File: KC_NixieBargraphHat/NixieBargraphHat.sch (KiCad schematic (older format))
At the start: 16 parts, among them J1 Screw_Terminal_1x03, J2 Screw_Terminal_1x02, Q1 FDD18N20LZ, Q2 2N7002, U1 MCP6411, U2 Raspberry_PI_Zero_Header

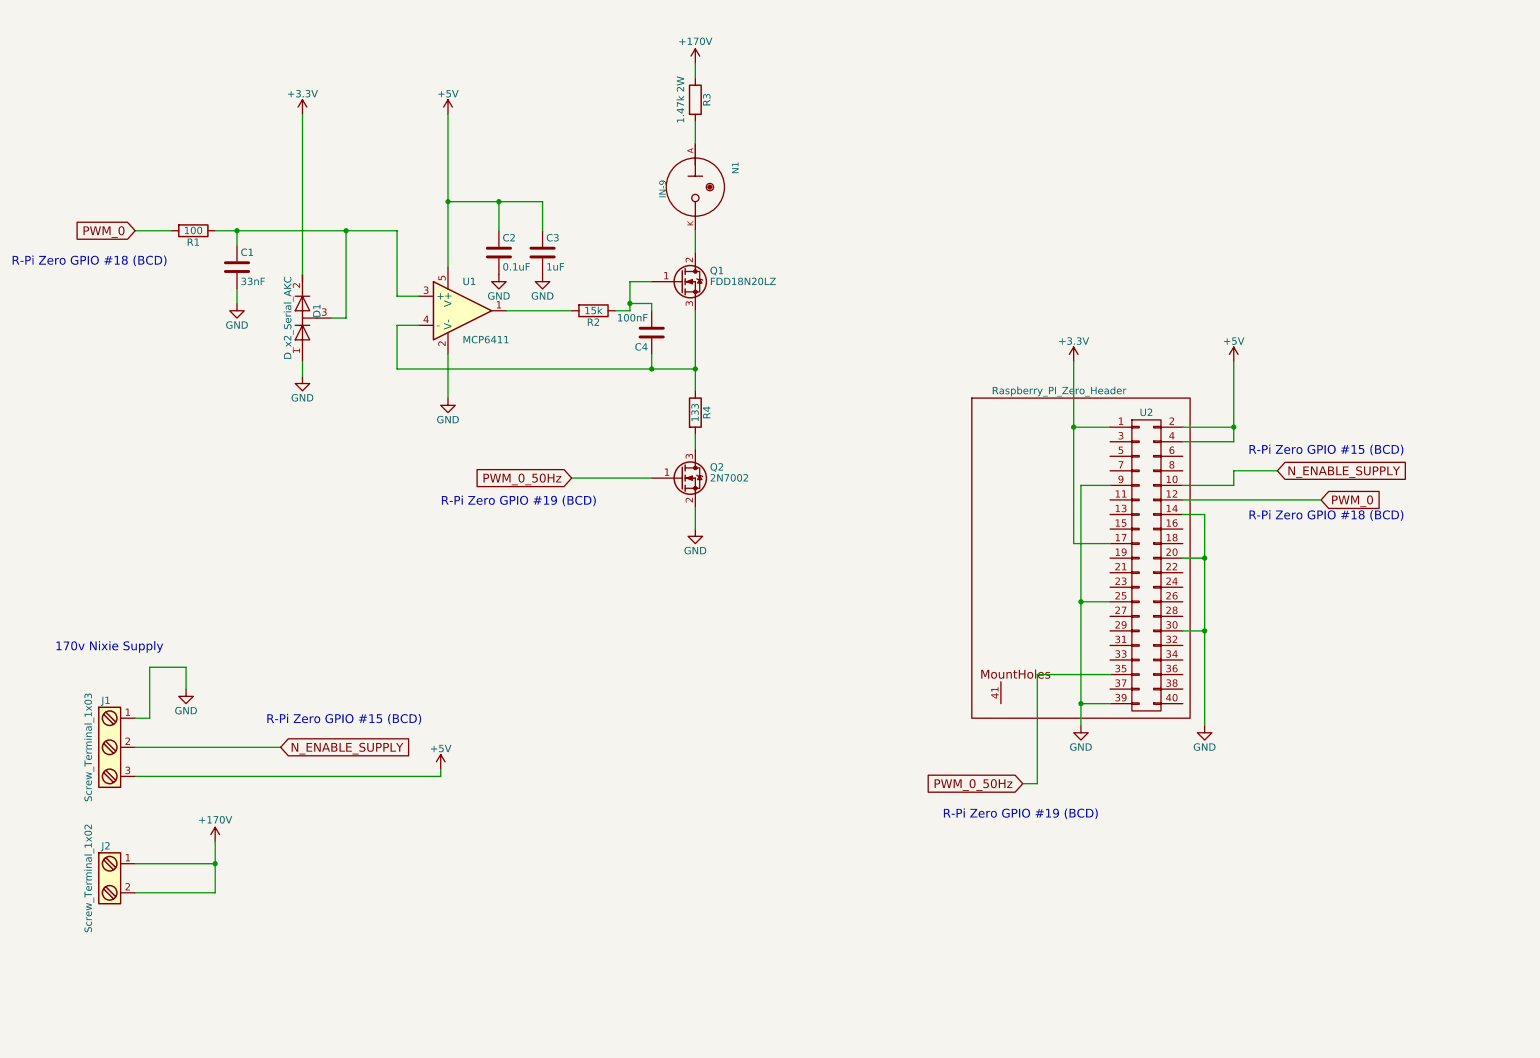
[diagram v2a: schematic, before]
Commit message: Adjusted the schematic to have two channels for the Left and Right Nixie. Also adjusted the PWM to have hardware PWM for the cathod signals, but the low frequency dimming will be done with the 50 Hz low frequency signals
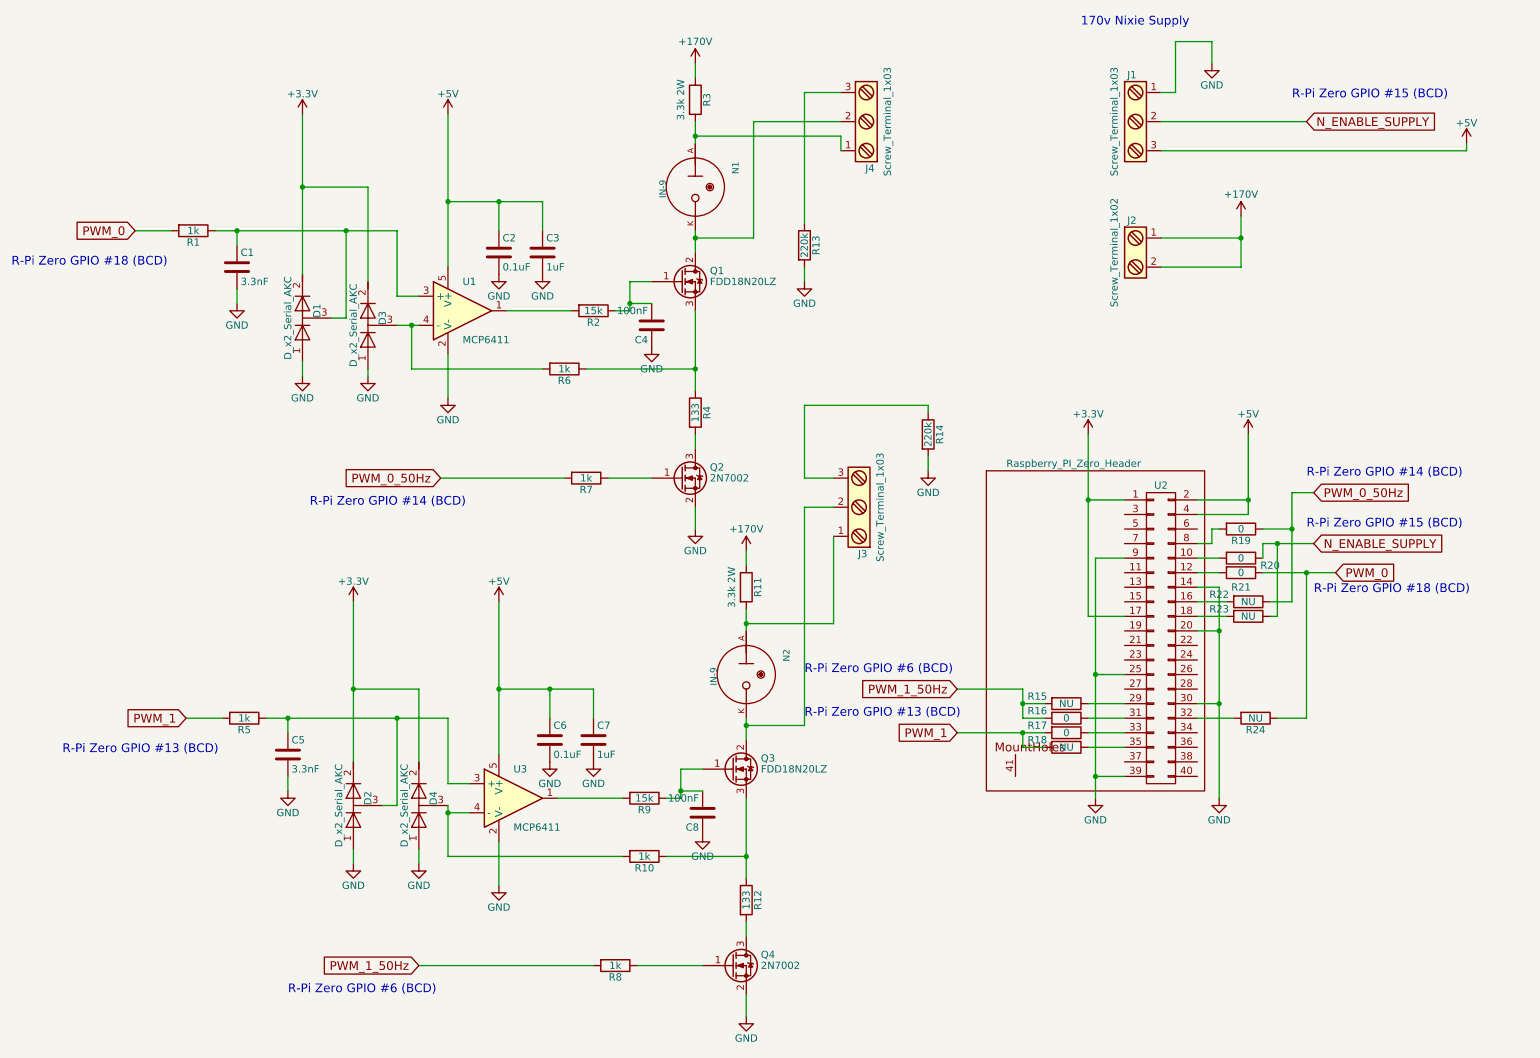
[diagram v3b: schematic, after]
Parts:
- added C5: 3.3nF, symbol C
- added C6: 0.1uF, symbol C
- added C7: 1uF, symbol C
- added C8: 100nF, symbol C
- added D2, D3, D4: D_x2_Serial_AKC, symbol D_x2_Serial_AKC
- added J3, J4: Screw_Terminal_1x03, symbol Screw_Terminal_1x03
- added N2: IN-9, nixies-us_IN-9, symbol IN-9
- added Q3: FDD18N20LZ, TO_SOT_Packages_SMD:SOT-223-3Lead_TabPin2, symbol BSP129
- added Q4: 2N7002, TO_SOT_Packages_SMD:SOT-23, symbol 2N7002
- added R10, R5, R6, R7, R8: 1k, symbol R
- added R11: 3.3k 2W, symbol R
- added R12: 133, symbol R
- added R13, R14: 220k, symbol R
- added R15, R18, R22, R23, R24: NU, symbol R
- added R16, R17, R19, R20, R21: 0, symbol R
- added R9: 15k, symbol R
- added U3: MCP6411, symbol MCP6001
- C1: value 33nF -> 3.3nF
- R1: value 100 -> 1k
- R3: value 1.47k 2W -> 3.3k 2W
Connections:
- net +170V: now also R11.1
- net +3V3: now also D2.2 (K), D3.2 (K), D4.2 (K)
- net +5V: now also C6.1, C7.1, U3.5 (V+)
- net GND: now also C4.1, C5.2, C6.2, C7.2, C8.1, D2.1 (A), D3.1 (A), D4.1 (A), Q4.2 (S), R13.2, R14.2, U3.2 (V-)
- net N_ENABLE_SUPPLY: now also R20.1, R23.1; no longer U2.10 (P10)
- net PWM_0: now also R21.1, R24.1; no longer U2.12 (P12)
- net PWM_0_50Hz: now also R19.1, R22.1, R7.2; no longer Q2.1 (G), U2.35 (P35)
- net at Q1.3 (S), R4.1: now also R6.1; no longer C4.1, U1.4 (-)
- net at N1.A, R3.2: now also J4.1
- net at N1.K, Q1.2 (D): now also J4.2
- net at U2.16 (P16): now also R22.2
- net at U2.18 (P18): now also R23.2
- net at U2.29 (P29): now also R15.1
- net at U2.31 (P31): now also R16.1
- net at U2.32 (P32): now also R24.2
- net at U2.33 (P33): now also R17.1
- net at U2.8 (P8): now also R19.2
- new net: D3.3 (common), R6.2, U1.4 (-)
- new net: Q2.1 (G), R7.1
- new net: R20.2, U2.10 (P10)
- new net: R21.2, U2.12 (P12)
- new net: R18.1, U2.35 (P35)
- new net: C5.1, D2.3 (common), R5.1, U3.3 (+)
- new net: Q3.3 (S), R10.1, R12.1
- new net: Q4.3 (D), R12.2
- new net: C8.2, Q3.1 (G), R9.1
- new net: R9.2, U3.1
- new net: J3.1, N2.A, R11.2
- new net: Q4.1 (G), R8.1
- new net: J3.2, N2.K, Q3.2 (D)
- new net: D4.3 (common), R10.2, U3.4 (-)
- new net: J4.3, R13.1
- new net: J3.3, R14.1
- new net PWM_1: R17.2, R18.2, R5.2
- new net PWM_1_50Hz: R15.2, R16.2, R8.2
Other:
- note added: "R-Pi Zero GPIO #13 (BCD)"
- note added: "R-Pi Zero GPIO #14 (BCD)"
- note added: "R-Pi Zero GPIO #6 (BCD)"
- note removed: "R-Pi Zero GPIO #19 (BCD)"
- moved on the sheet: C4, J1, J2, U2

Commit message: updated the schematic to include a feedback for op-amp to avoid oscillation
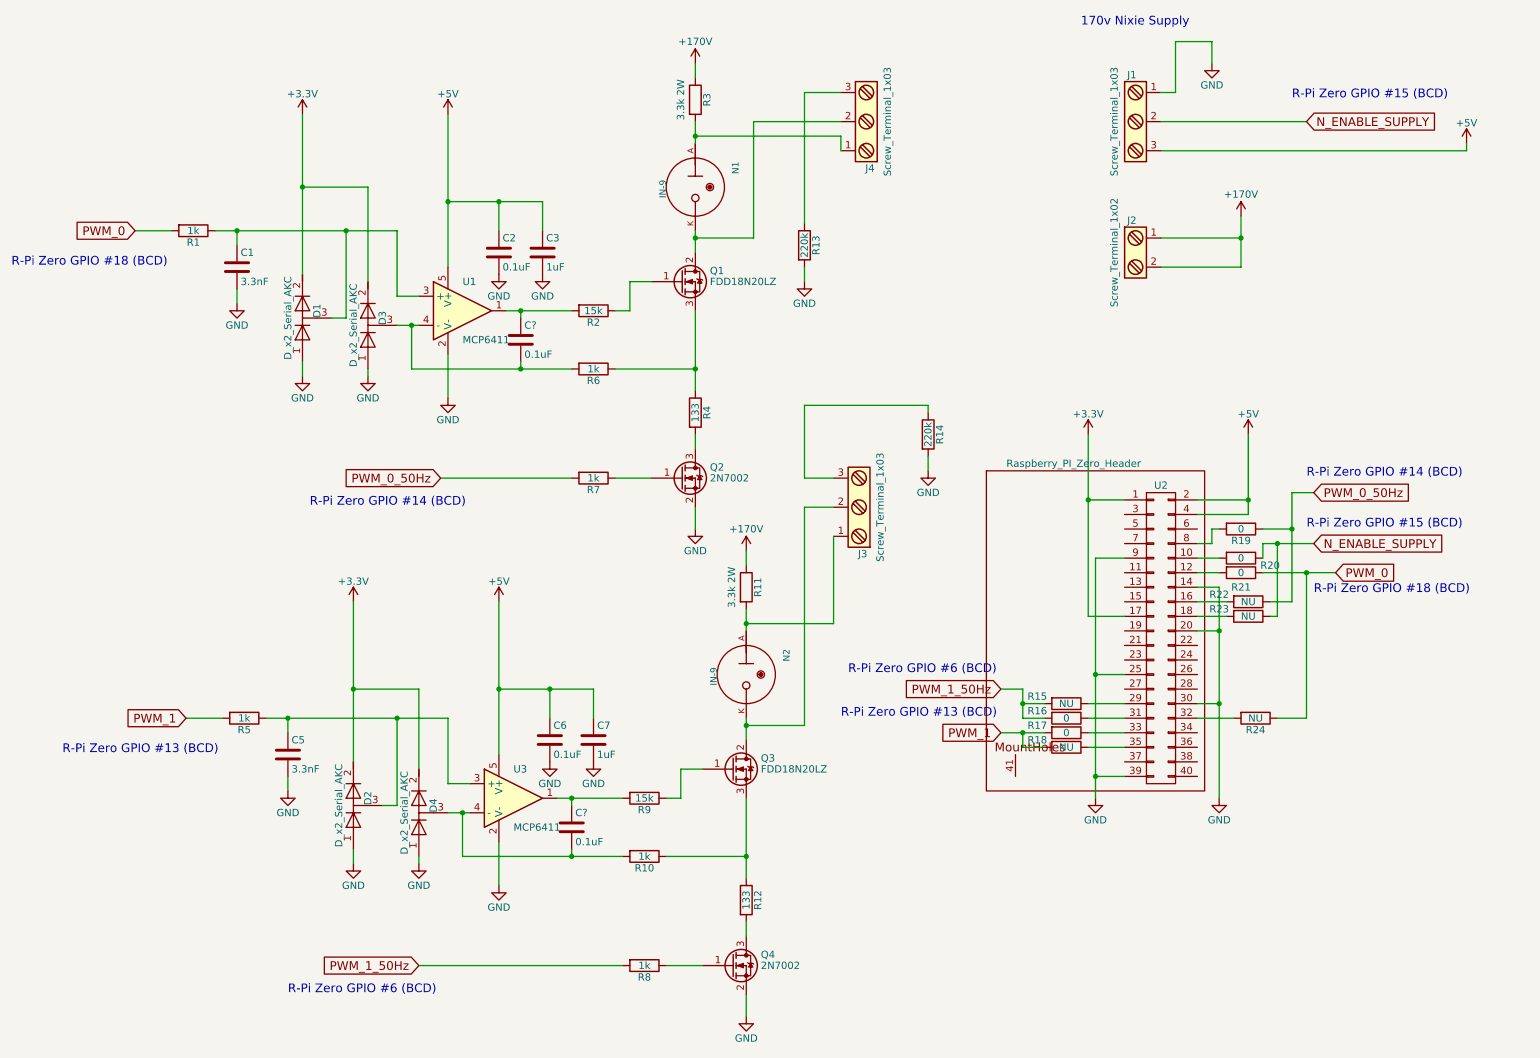
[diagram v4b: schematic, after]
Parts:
- removed C4, C8: 100nF, symbol C
- added C? (x2): 0.1uF, symbol C
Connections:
- net at R2.2, U1.1: now also C?.1
- net at D3.3 (common), R6.2, U1.4 (-): now also C?.2
- net at R9.2, U3.1: now also C?.1
- net at D4.3 (common), R10.2, U3.4 (-): now also C?.2
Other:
- moved on the sheet: D4, R6, R7, R8
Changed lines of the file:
@@
-$EndComp
-$Comp
-L C C4
-U 1 1 5BCD5690
-P 5350 2750
-F 0 "C4" H 5375 2850 50  0000 L CNN
-F 1 "100nF" H 5375 2650 50  0000 L CNN
-F 2 "" H 5388 2600 50  0001 C CNN
-F 3 "" H 5350 2750 50  0001 C CNN
-	1    5350 2750
-	-1   0    0    1
 $EndComp
 $Comp
@@
 	5650 3500 5650 3600
 Wire Wire Line
-	4350 2650 4800 2650
+	4350 2650 4450 2650
+Wire Wire Line
+	4450 2650 4800 2650
 Wire Wire Line
 	2350 2100 2500 2100
@@
 	3950 3250 3950 2950
 Wire Wire Line
-	3900 3800 4750 3800
+	3900 3800 4800 3800
 Wire Wire Line
 	5650 950  5650 1050
@@
 	5200 2650 5100 2650
 Wire Wire Line
-	5200 2450 5200 2600
-Wire Wire Line
-	5200 2600 5200 2650
+	5200 2450 5200 2650
 Wire Wire Line
 	5200 2450 5350 2450
-Wire Wire Line
-	5200 2600 5350 2600
-Connection ~ 5200 2600
 $Comp
 L C C2
@@
 	1    5900 7150
 	1    0    0    -1
-$EndComp
-$Comp
-L C C8
-U 1 1 5C3BFF78
-P 5700 6100
-F 0 "C8" H 5725 6200 50  0000 L CNN
-F 1 "100nF" H 5725 6000 50  0000 L CNN
-F 2 "" H 5738 5950 50  0001 C CNN
-F 3 "" H 5700 6100 50  0001 C CNN
-	1    5700 6100
-	-1   0    0    1
 $EndComp
 $Comp
@@
 	6000 6850 6000 6950
 Wire Wire Line
-	4700 6000 5150 6000
+	4700 6000 4800 6000
+Wire Wire Line
+	4800 6000 5150 6000
 Wire Wire Line
 	2700 5450 2850 5450
@@
 	3950 5900 4100 5900
 Wire Wire Line
-	4100 6100 3950 6100
-Wire Wire Line
-	3950 6050 3950 6100
-Wire Wire Line
-	3950 6100 3950 6400
+	4100 6100 4050 6100
+Wire Wire Line
+	4050 6100 3950 6100
+Wire Wire Line
+	4050 6100 4050 6400
 Connection ~ 6000 6400
 Wire Wire Line
@@
 	4300 6600 4300 6300
 Wire Wire Line
-	3750 7150 4950 7150
+	3750 7150 5150 7150
 Wire Wire Line
 	6000 4300 6000 4400
@@
 	5550 6000 5450 6000
 Wire Wire Line
-	5550 5800 5550 5950
-Wire Wire Line
-	5550 5950 5550 6000
+	5550 5800 5550 6000
 Wire Wire Line
 	5550 5800 5700 5800
-Wire Wire Line
-	5550 5950 5700 5950
-Connection ~ 5550 5950
 $Comp
 L C C6
@@
 Wire Wire Line
 	9750 3900 9900 3900
-Text GLabel 7450 5550 0    60   Input ~ 0
+Text GLabel 7750 5550 0    60   Input ~ 0
 PWM_1
-Text Notes 6400 5450 0    60   ~ 0
+Text Notes 6650 5450 0    60   ~ 0
 R-Pi Zero GPIO #13 (BCD)
-Text Notes 6400 5150 0    60   ~ 0
+Text Notes 6700 5150 0    60   ~ 0
 R-Pi Zero GPIO #6 (BCD)
-Text GLabel 7450 5250 0    60   Input ~ 0
+Text GLabel 7750 5250 0    60   Input ~ 0
 PWM_1_50Hz
 Wire Wire Line
@@
 	7900 5350 7900 5450
 Wire Wire Line
-	7900 5250 7450 5250
-$Comp
-L GND #PWR20
-U 1 1 5C3C231E
-P 5700 6250
-F 0 "#PWR20" H 5700 6000 50  0001 C CNN
-F 1 "GND" H 5700 6100 50  0000 C CNN
-F 2 "" H 5700 6250 50  0001 C CNN
-F 3 "" H 5700 6250 50  0001 C CNN
-	1    5700 6250
-	1    0    0    -1
-$EndComp
+	7900 5250 7750 5250
 Wire Wire Line
 	5700 6250 5700 6250
-$Comp
-L GND #PWR17
-U 1 1 5C3C2641
-P 5350 2900
-F 0 "#PWR17" H 5350 2650 50  0001 C CNN
-F 1 "GND" H 5350 2750 50  0000 C CNN
-F 2 "" H 5350 2900 50  0001 C CNN
-F 3 "" H 5350 2900 50  0001 C CNN
-	1    5350 2900
-	1    0    0    -1
-$EndComp
 Wire Wire Line
 	5350 2900 5350 2900
@@
 L R R6
 U 1 1 5C3C2790
-P 4750 3050
-F 0 "R6" V 4830 3050 50  0000 C CNN
-F 1 "1k" V 4750 3050 50  0000 C CNN
-F 2 "" V 4680 3050 50  0001 C CNN
-F 3 "" H 4750 3050 50  0001 C CNN
-	1    4750 3050
-	0    1    1    0
-$EndComp
-Wire Wire Line
-	4900 3050 5650 3050
+P 4950 3050
+F 0 "R6" V 5030 3050 50  0000 C CNN
+F 1 "1k" V 4950 3050 50  0000 C CNN
+F 2 "" V 4880 3050 50  0001 C CNN
+F 3 "" H 4950 3050 50  0001 C CNN
+	1    4950 3050
+	0    1    1    0
+$EndComp
+Wire Wire Line
+	5100 3050 5650 3050
 $Comp
 L R R10
@@
 	5450 6400 6000 6400
 Wire Wire Line
-	3950 6400 5150 6400
+	4050 6400 4800 6400
+Wire Wire Line
+	4800 6400 5150 6400
 $Comp
 L R R8
 U 1 1 5C3C2FE6
-P 5100 7150
-F 0 "R8" V 5180 7150 50  0000 C CNN
-F 1 "1k" V 5100 7150 50  0000 C CNN
-F 2 "" V 5030 7150 50  0001 C CNN
-F 3 "" H 5100 7150 50  0001 C CNN
-	1    5100 7150
-	0    1    1    0
-$EndComp
-Wire Wire Line
-	5250 7150 5700 7150
+P 5300 7150
+F 0 "R8" V 5380 7150 50  0000 C CNN
+F 1 "1k" V 5300 7150 50  0000 C CNN
+F 2 "" V 5230 7150 50  0001 C CNN
+F 3 "" H 5300 7150 50  0001 C CNN
+	1    5300 7150
+	0    1    1    0
+$EndComp
+Wire Wire Line
+	5450 7150 5700 7150
 $Comp
 L R R7
 U 1 1 5C3C328B
-P 4900 3800
-F 0 "R7" V 4980 3800 50  0000 C CNN
-F 1 "1k" V 4900 3800 50  0000 C CNN
-F 2 "" V 4830 3800 50  0001 C CNN
-F 3 "" H 4900 3800 50  0001 C CNN
-	1    4900 3800
-	0    1    1    0
-$EndComp
-Wire Wire Line
-	5050 3800 5350 3800
+P 4950 3800
+F 0 "R7" V 5030 3800 50  0000 C CNN
+F 1 "1k" V 4950 3800 50  0000 C CNN
+F 2 "" V 4880 3800 50  0001 C CNN
+F 3 "" H 4950 3800 50  0001 C CNN
+	1    4950 3800
+	0    1    1    0
+$EndComp
+Wire Wire Line
+	5100 3800 5350 3800
 $Comp
 L Screw_Terminal_1x03 J4
@@
 Connection ~ 3700 2750
 Wire Wire Line
-	3700 3050 4600 3050
+	3700 3050 4450 3050
+Wire Wire Line
+	4450 3050 4800 3050
 $Comp
 L D_x2_Serial_AKC D4
 U 1 1 5C3C67CE
-P 3750 6050
-F 0 "D4" H 3800 5950 50  0000 C CNN
-F 1 "D_x2_Serial_AKC" H 3750 6150 50  0000 C CNN
-F 2 "" H 3750 6050 50  0001 C CNN
-F 3 "https://www.digikey.com/product-detail/en/nexperia-usa-inc/BAV99235/1727-4311-1-ND/2209921" H 3750 6050 50  0001 C CNN
-	1    3750 6050
+P 3750 6100
+F 0 "D4" H 3800 6000 50  0000 C CNN
+F 1 "D_x2_Serial_AKC" H 3750 6200 50  0000 C CNN
+F 2 "" H 3750 6100 50  0001 C CNN
+F 3 "https://www.digikey.com/product-detail/en/nexperia-usa-inc/BAV99235/1727-4311-1-ND/2209921" H 3750 6100 50  0001 C CNN
+	1    3750 6100
 	0    -1   -1   0
 $EndComp
@@
 $EndComp
 Wire Wire Line
-	3750 6450 3750 6350
+	3750 6450 3750 6400
 Wire Wire Line
 	3300 5250 3750 5250
 Wire Wire Line
-	3750 5250 3750 5750
+	3750 5250 3750 5800
 Connection ~ 3300 5250
-Connection ~ 3950 6100
+Connection ~ 4050 6100
 $Comp
 L R R16
@@
 $EndComp
 Wire Wire Line
-	7450 5550 7900 5550
+	7750 5550 7900 5550
 Wire Wire Line
 	7900 5550 8050 5550
@@
 	9650 4750 9650 4250
 Connection ~ 9650 4250
+$Comp
+L C C?
+U 1 1 5C3D8CCB
+P 4450 2850
+F 0 "C?" H 4475 2950 50  0000 L CNN
+F 1 "0.1uF" H 4475 2750 50  0000 L CNN
+F 2 "" H 4488 2700 50  0001 C CNN
+F 3 "" H 4450 2850 50  0001 C CNN
+	1    4450 2850
+	1    0    0    -1
+$EndComp
+Wire Wire Line
+	4450 3000 4450 3050
+Connection ~ 4450 3050
+Wire Wire Line
+	4450 2700 4450 2650
+Connection ~ 4450 2650
+$Comp
+L C C?
+U 1 1 5C3D913D
+P 4800 6200
+F 0 "C?" H 4825 6300 50  0000 L CNN
+F 1 "0.1uF" H 4825 6100 50  0000 L CNN
+F 2 "" H 4838 6050 50  0001 C CNN
+F 3 "" H 4800 6200 50  0001 C CNN
+	1    4800 6200
+	1    0    0    -1
+$EndComp
+Wire Wire Line
+	4800 6050 4800 6000
+Connection ~ 4800 6000
+Wire Wire Line
+	4800 6350 4800 6400
+Connection ~ 4800 6400
 $EndSCHEMATC
